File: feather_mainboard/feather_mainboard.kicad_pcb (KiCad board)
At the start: 2 copper layers, 0 parts

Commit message: added daughter board
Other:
- board outline added: 60 x 60 mm
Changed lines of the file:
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@@
 				(material "Peters SD2692")
 			)
-			(copper_finish "HAL lead-free")
+			(copper_finish "ENIG")
 			(dielectric_constraints no)
 		)
@@
 	)
 	(net 0 "")
+	(gr_line
+		(start 170 125)
+		(end 110 125)
+		(stroke
+			(width 0.05)
+			(type default)
+		)
+		(layer "Edge.Cuts")
+	)
+	(gr_line
+		(start 110 65)
+		(end 170 65)
+		(stroke
+			(width 0.05)
+			(type default)
+		)
+		(layer "Edge.Cuts")
+	)
+	(gr_line
+		(start 110 125)
+		(end 110 65)
+		(stroke
+			(width 0.05)
+			(type default)
+		)
+		(layer "Edge.Cuts")
+	)
+	(gr_line
+		(start 170 65)
+		(end 170 125)
+		(stroke
+			(width 0.05)
+			(type default)
+		)
+		(layer "Edge.Cuts")
+	)
 )

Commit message: finished mainboard design, need to do the routing
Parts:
- added C1_1: 100nF, Custom footprints:WCAP-CSGP_0603_R, F.Cu at (134.9, 107.7)
- added C1_2: 100nF, Custom footprints:WCAP-CSGP_0603_R, F.Cu at (131.7, 107.7)
- added C1_3: 100nF, Custom footprints:WCAP-CSGP_0603_R, F.Cu at (128.4, 107.8)
- added C1_4: 100nF, Custom footprints:WCAP-CSGP_0603_R, F.Cu at (139.7, 80.8)
- added C2_1: 10µF, Custom footprints:WCAP-CSGP_1210_H2.0, F.Cu at (167.1, 82.3)
- added C2_2: 10µF, Custom footprints:WCAP-CSGP_0603_R, F.Cu at (139.7, 83.9)
- added C3: 470pF, Custom footprints:WCAP-CSMH_1808_H2.0, F.Cu at (160.6, 95.6)
- added C4_1: 4.7µF, Custom footprints:WCAP-CSGP_1210_H2.0, F.Cu at (151.9, 95.3)
- added C4_2: 4.7µF, Custom footprints:WCAP-CSGP_1210_H2.0, F.Cu at (145.5, 81.7)
- added G***: LOGO, Custom footprints:Logo, F.Cu at (147.5, 72.9)
- added G***: LOGO, Custom footprints:Logo, B.Cu at (147.4, 72.9)
- added H1: MountingHole_Pad, MountingHole:MountingHole_2.2mm_M2_DIN965_Pad, F.Cu at (176.6, 73.1)
- added H2: MountingHole_Pad, MountingHole:MountingHole_2.2mm_M2_DIN965_Pad, F.Cu at (123.4, 73.1)
- added H3: MountingHole_Pad, MountingHole:MountingHole_2.2mm_M2_DIN965_Pad, F.Cu at (176.6, 126.3)
- added H4: MountingHole_Pad, MountingHole:MountingHole_2.2mm_M2_DIN965_Pad, F.Cu at (123.4, 126.3)
- added IIC: 61300211121, Custom footprints:61300211121, F.Cu at (172.5, 82.8)
- added J1: 61900819521, Custom footprints:61900819521, F.Cu at (160.9, 71.8)
- added J2: 61900619521, Custom footprints:61900619521, F.Cu at (136.4, 71.8)
- added J4: 693071020811, Custom footprints:693071020811, F.Cu at (124.3, 89.4)
- added L1: 6.8µH, Custom footprints:WE-PD2_4532, F.Cu at (146.2, 89.2)
- added R1_1: 10kΩ, Custom footprints:WRIS-RSKS_0603_REFLOW, F.Cu at (162.1, 107.5)
- added R1_10: 10kΩ, Custom footprints:WRIS-RSKS_0603_REFLOW, F.Cu at (140.4, 115.8)
- added R1_11: 10kΩ, Custom footprints:WRIS-RSKS_0603_REFLOW, F.Cu at (143.4, 115.8)
- added R1_2: 10kΩ, Custom footprints:WRIS-RSKS_0603_REFLOW, F.Cu at (144.9, 107.6)
- added R1_3: 10kΩ, Custom footprints:WRIS-RSKS_0603_REFLOW, F.Cu at (150.4, 115.8)
- added R1_4: 10kΩ, Custom footprints:WRIS-RSKS_0603_REFLOW, F.Cu at (153.4, 115.8)
- added R1_5: 10kΩ, Custom footprints:WRIS-RSKS_0603_REFLOW, F.Cu at (159.1, 115.8)
- added R1_6: 10kΩ, Custom footprints:WRIS-RSKS_0603_REFLOW, F.Cu at (128.4, 115.8)
- added R1_7: 10kΩ, Custom footprints:WRIS-RSKS_0603_REFLOW, F.Cu at (131.4, 115.8)
- added R1_8: 10kΩ, Custom footprints:WRIS-RSKS_0603_REFLOW, F.Cu at (134.4, 115.8)
- added R1_9: 10kΩ, Custom footprints:WRIS-RSKS_0603_REFLOW, F.Cu at (137.4, 115.8)
- added R2_1: 180Ω, Custom footprints:WRIS-RSKS_0603_REFLOW, F.Cu at (147.9, 107.6)
- added R3_1: 75kΩ, Custom footprints:WRIS-RSKS_0603_REFLOW, F.Cu at (162.1, 115.8)
- added RST: 61300211121, Custom footprints:61300211121, F.Cu at (144.3, 96.6)
- added S1: 450406020024, Custom footprints:450406020024, F.Cu at (169.8, 92.2)
- added SD: 61300211121, Custom footprints:61300211121, F.Cu at (139.8, 89.7)
- added U1: Adafruit ESP32-S3 Feather, Custom footprints:Adafruit ESP32-S3 Feather 4MB Flash 2MB PSRAM, F.Cu at (144.4, 95.7)
- added U2: SI2307CDS-T1-BE3, Custom footprints:SOT-23_VIS, F.Cu at (157.8, 107.6)
- added U3: 2N7002K-T1-GE3, Custom footprints:SOT_02K-T1-GE3_VIS, F.Cu at (152.3, 107.6)
- added U4: WPME-FISM_SMT-8, Custom footprints:WPME-FISM_SMT-8_L13.2W11.4H7.25, F.Cu at (156.6, 86.4)
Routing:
- added copper zone on B.Cu, net GND
- added copper zone on F.Cu, net GND
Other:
- board text added: "3.3V"
- board text added: "5V"
- board text added: "BUSY"
- board text added: "B_1"
- board text added: "B_2"
- board text added: "B_3"
- board text added: "B_4"
- board text added: "CLK"
- board text added: "CS"
- board text added: "DC"
- board text added: "DIN"
- board text added: "Do not connect"
- board text added: "GND"
- board text added: "IIC"
- board text added: "LPRD_Feather_MainBoard_V1"
- board text added: "RST"
- board text added: "SCL"
- board text added: "SDA"
- board text added: "TI_WiSe_2024/25"
- board text added: "VCC"

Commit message: finished the mainboard, added bom files
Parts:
- moved H2 0.36 mm to (123.2, 72.8)
- moved H4 0.36 mm to (123.2, 126.0)
- moved H1 0.36 mm to (176.4, 72.8)
- moved H3 0.36 mm to (176.4, 126.0)
- moved R1_1 0.30 mm to (162.4, 107.5)
- moved R1_5 0.30 mm to (159.4, 115.8)
- moved R1_6 0.30 mm to (128.7, 115.8)
- moved U1 0.30 mm to (144.7, 95.7)
- moved R1_2 0.30 mm to (145.2, 107.7)
- moved R2_1 0.30 mm to (148.2, 107.7)
- moved U2 0.30 mm to (158.1, 107.7)
- moved U3 0.30 mm to (152.6, 107.7)
- moved C1_1 0.30 mm to (135.2, 107.8)
- moved C1_2 0.30 mm to (131.9, 107.8)
- moved C1_3 0.30 mm to (128.7, 107.8)
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- renumbered G*** to G**
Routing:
- net /MicroSD-Card Adapter/SD_DAT1: track 0.00 -> 77.3 mm, vias 0 -> 1
- net /Display-Ports/SCLK: track 0.00 -> 71.9 mm, vias 0 -> 1
- net VCC: track 0.00 -> 68.4 mm
- net /MicroSD-Card Adapter/SD_CD: track 0.00 -> 68.4 mm, vias 0 -> 1
- net /Display-Ports/DIN: track 0.00 -> 67.9 mm
- net /Buttons-Connector/Button_1: track 0.00 -> 59.8 mm
- net /Buttons-Connector/Button_2: track 0.00 -> 57.3 mm
- net /Display-Enable/Switch: track 0.00 -> 56.8 mm
- net /Buttons-Connector/Button_4: track 0.00 -> 55.5 mm
- net /MicroSD-Card Adapter/SD_DAT2: track 0.00 -> 55.3 mm
- net /Display-Ports/RST: track 0.00 -> 55.2 mm
- net /Microcontroller/Reset: track 0.00 -> 54.8 mm
- net /Display-Ports/CS: track 0.00 -> 52.4 mm
- net /MicroSD-Card Adapter/SD_MOSI/DAT0: track 0.00 -> 52.0 mm, vias 0 -> 1
- net /Buttons-Connector/Button_3: track 0.00 -> 50.1 mm
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
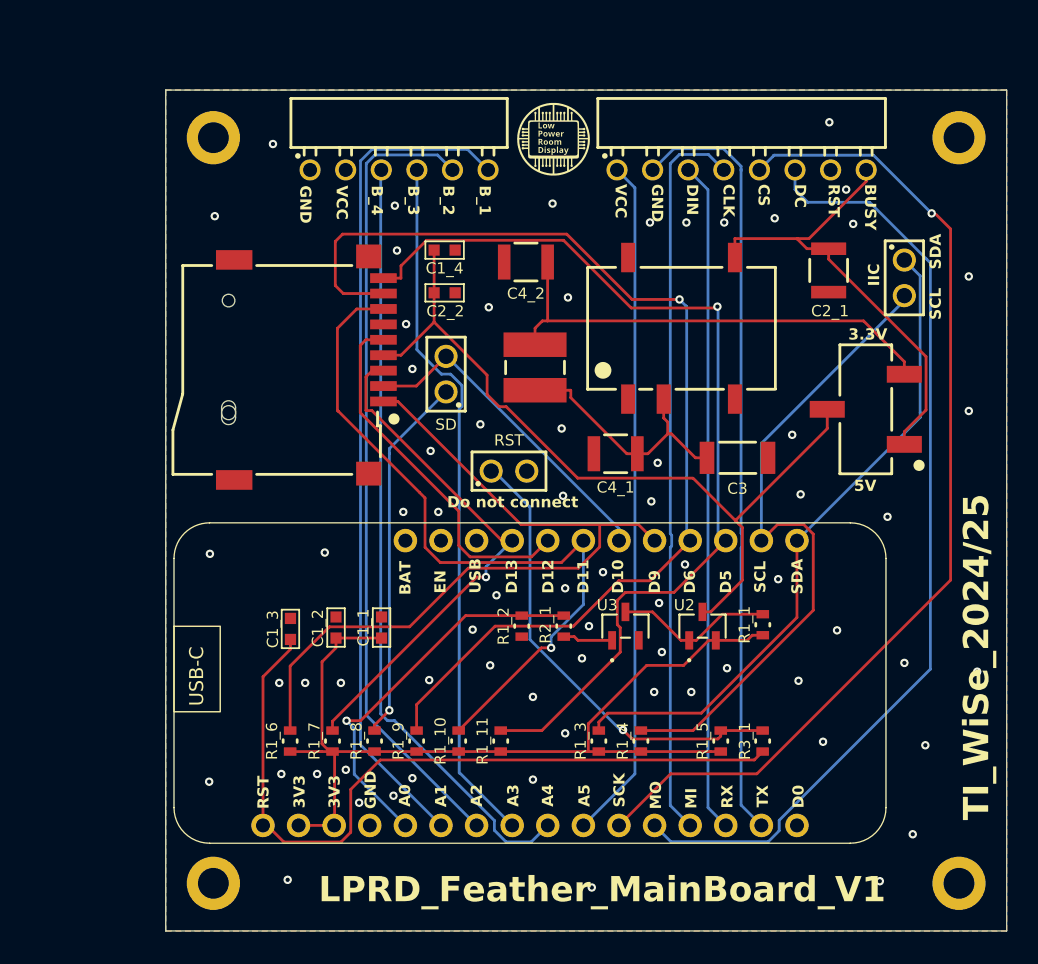
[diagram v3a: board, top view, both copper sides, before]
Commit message: moved the logo and did some small changes
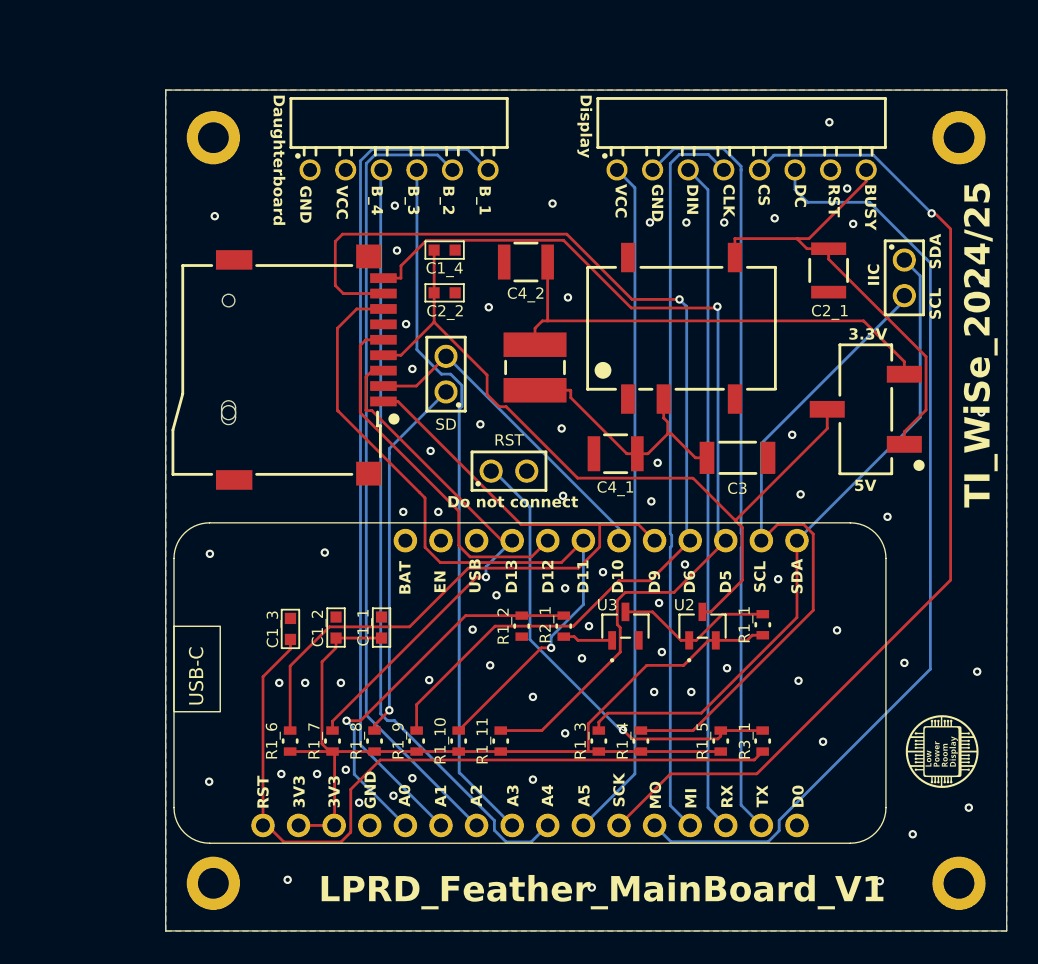
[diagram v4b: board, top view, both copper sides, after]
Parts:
- moved G*** 51.8 mm to (175.2, 116.6), turned to -90 degrees
- moved G** 51.7 mm to (175.2, 116.6), turned to 90 degrees
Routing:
- net GND: vias 69 -> 68
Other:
- board text added: "Daughterboard"
- board text added: "Display"

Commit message: added pins for the sd connections
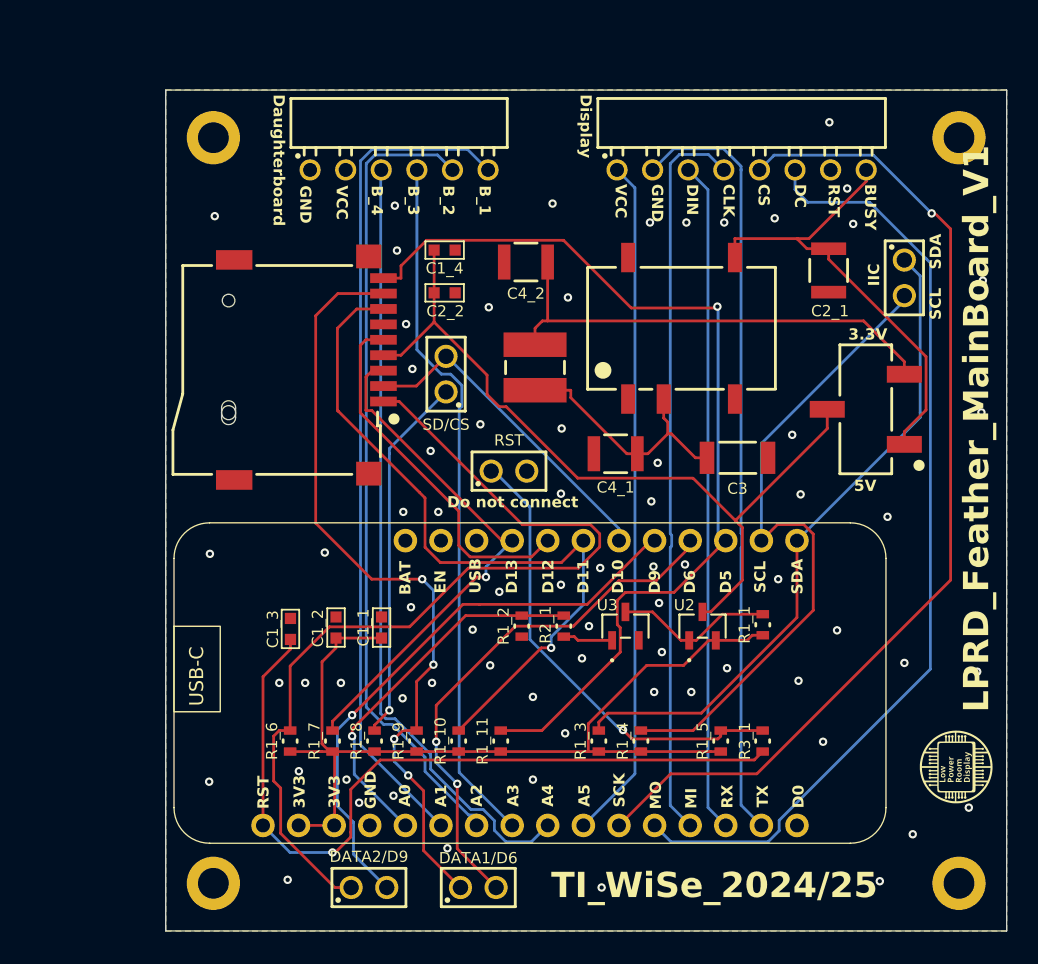
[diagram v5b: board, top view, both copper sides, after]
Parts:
- added DATA1/D6: 61300211121, Custom footprints:61300211121, F.Cu at (142.1, 126.3)
- added DATA2/D9: 61300211121, Custom footprints:61300211121, F.Cu at (134.3, 126.3)
- moved G** 1.49 mm to (176.2, 117.7)
- moved G*** 1.49 mm to (176.2, 117.7)
- renumbered SD to SD/CS
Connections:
- J4 pad 1: /MicroSD-Card Adapter/SD_DAT2 -> Net-(J4-DAT2)
- J4 pad 8: /MicroSD-Card Adapter/SD_DAT1 -> Net-(J4-DAT1)
- R1_6 pad 1: /MicroSD-Card Adapter/SD_DAT2 -> Net-(J4-DAT2)
- R1_9 pad 2: /MicroSD-Card Adapter/SD_DAT1 -> Net-(J4-DAT1)
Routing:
- net Net-(J4-DAT2): track 0.00 -> 65.6 mm
- net Net-(J4-DAT1): track 0.00 -> 55.6 mm, vias 0 -> 4
- net /MicroSD-Card Adapter/SD_DAT1: track 77.3 -> 38.4 mm, vias 1 -> 2
- net /MicroSD-Card Adapter/SD_DAT2: track 55.3 -> 40.9 mm, vias 0 -> 1
- net /Display-Enable/EN: track 28.0 -> 27.1 mm
- net /Buttons-Connector/Button_2: track 57.3 -> 58.0 mm
- net /Microcontroller/Reset: track 54.8 -> 55.5 mm, vias 0 -> 1
- net /Buttons-Connector/Button_4: track 55.5 -> 56.1 mm
- net GND: vias 68 -> 70

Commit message: changed the connector on the daughter board
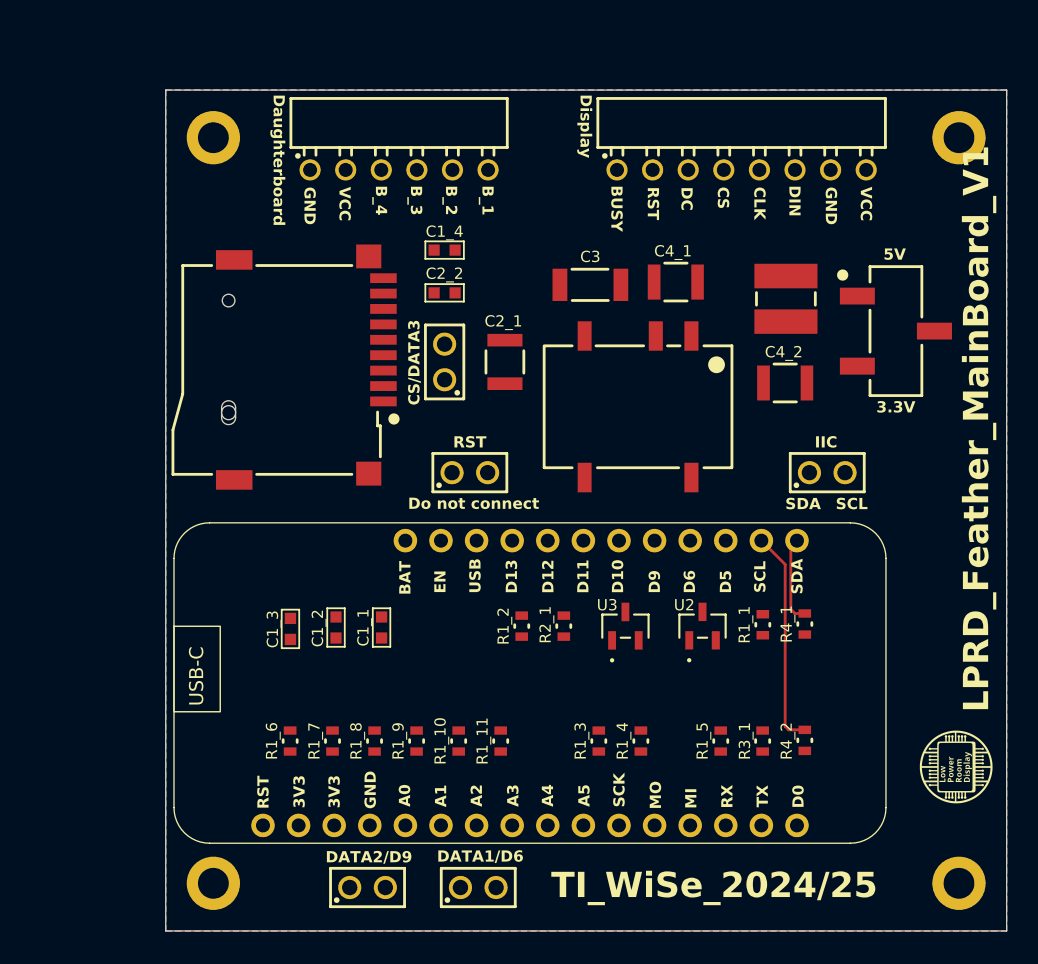
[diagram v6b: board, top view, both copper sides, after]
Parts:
- removed DATA1/D6, DATA2/D9, IIC, RST, SD/CS: 61300211121, Custom footprints:61300211121
- added J3: 61300211121, Custom footprints:61300211121, F.Cu at (141.5, 96.7)
- added J5: 61300211121, Custom footprints:61300211121, F.Cu at (139.7, 88.8)
- added J6: 61300211121, Custom footprints:61300211121, F.Cu at (167.0, 96.7)
- added J7: 61300211121, Custom footprints:61300211121, F.Cu at (134.2, 126.3)
- added J8: 61300211121, Custom footprints:61300211121, F.Cu at (142.1, 126.3)
- added R4_1: 33Ω, Custom footprints:WRIS-RSKS_0603_REFLOW, F.Cu at (165.4, 107.5)
- added R4_2: 33Ω, Custom footprints:WRIS-RSKS_0603_REFLOW, F.Cu at (165.4, 115.8)
- moved C2_1 24.0 mm to (144.0, 88.8), turned to 90 degrees
- moved C4_2 20.4 mm to (164.0, 90.3)
- moved L1 18.6 mm to (164.1, 84.3)
- moved C3 16.2 mm to (150.1, 83.3), turned to 180 degrees
- moved C4_1 13.0 mm to (156.2, 83.1), turned to 0 degrees
- moved U4 6.40 mm to (153.5, 92.0), turned to 180 degrees
- moved S1 5.98 mm to (171.9, 86.6), turned to -90 degrees
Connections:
- J2 pad 1: /Buttons-Connector/GND -> GND
- J2 pad 2: /Buttons-Connector/VCC -> VCC
- R1_3 pad 1: /IIC/SDA -> Net-(J6-Pad1)
- R1_4 pad 1: /IIC/SCL -> Net-(J6-Pad2)
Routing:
- net /Display-Ports/SCLK: track 71.9 -> 0.00 mm, vias 1 -> 0
- net VCC: track 68.4 -> 0.00 mm
- net /MicroSD-Card Adapter/SD_CD: track 68.4 -> 0.00 mm, vias 1 -> 0
- net /Display-Ports/DIN: track 67.9 -> 0.00 mm
- net Net-(J4-DAT2): track 65.6 -> 0.00 mm
- net /Buttons-Connector/Button_1: track 59.8 -> 0.00 mm
- net /Buttons-Connector/Button_2: track 58.0 -> 0.00 mm
- net /Display-Enable/Switch: track 56.8 -> 0.00 mm
- net /Buttons-Connector/Button_4: track 56.1 -> 0.00 mm
- net Net-(J4-DAT1): track 55.6 -> 0.00 mm, vias 4 -> 0
- net /Microcontroller/Reset: track 55.5 -> 0.00 mm, vias 1 -> 0
- net /Display-Ports/RST: track 55.2 -> 0.00 mm
- net /Display-Ports/CS: track 52.4 -> 0.00 mm
- net /MicroSD-Card Adapter/SD_MOSI/DAT0: track 52.0 -> 0.00 mm, vias 1 -> 0
- net /Buttons-Connector/Button_3: track 50.1 -> 0.00 mm
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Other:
- board text added: "CS/DATA3"
- board text added: "DATA1/D6"
- board text added: "DATA2/D9"

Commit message: finished mainboard and daughterboard
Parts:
- J1: value 61900819521 -> 62501021721; footprint Custom footprints:61900819521 -> Custom footprints:62501021721
- J2: value 61900619521 -> 62501021721; footprint Custom footprints:61900619521 -> Custom footprints:62501021721
- moved J1 1.27 mm to (162.1, 72.2)
- moved J2 1.12 mm to (137.5, 72.2)
- moved C4_1 0.10 mm to (156.3, 83.1)
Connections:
- J1 pad 1: /Display-Ports/BUSY -> unconnected-(J1-Pad1)
- J1 pad 2: /Display-Ports/RST -> /Display-Ports/BUSY
- J1 pad 3: /Display-Ports/DC -> /Display-Ports/RST
- J1 pad 4: /Display-Ports/CS -> /Display-Ports/DC
- J1 pad 5: /Display-Ports/SCLK -> /Display-Ports/CS
- J1 pad 6: /Display-Ports/DIN -> /Display-Ports/SCLK
- J1 pad 7: GND -> /Display-Ports/DIN
- J1 pad 8: /Boost-Converter/VOUT+ -> GND
- J2 pad 1: GND -> unconnected-(J2-Pad1)
- J2 pad 2: VCC -> unconnected-(J2-Pad2)
- J2 pad 4: /Buttons-Connector/Button_3 -> GND
- J2 pad 5: /Buttons-Connector/Button_2 -> /Buttons-Connector/Button_3
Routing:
- net VCC: track 0.00 -> 142.3 mm
- net /Display-Enable/Switch: track 0.00 -> 91.9 mm
- net /Buttons-Connector/Button_4: track 0.00 -> 64.0 mm
- net /Microcontroller/Reset: track 0.00 -> 58.9 mm
- net /Display-Ports/DIN: track 0.00 -> 57.9 mm
- net /Display-Ports/SCLK: track 0.00 -> 54.3 mm
- net /MicroSD-Card Adapter/SD_CD: track 0.00 -> 54.2 mm
- net /Display-Ports/CS: track 0.00 -> 52.3 mm
- net Net-(J4-DAT1): track 0.00 -> 51.5 mm, vias 0 -> 3
- net /Display-Ports/BUSY: track 0.00 -> 50.8 mm
- net /Buttons-Connector/Button_1: track 0.00 -> 48.4 mm
- net /Display-Ports/DC: track 0.00 -> 47.3 mm
- net /Buttons-Connector/Button_3: track 0.00 -> 47.1 mm, vias 0 -> 1
- net /Buttons-Connector/Button_2: track 0.00 -> 46.7 mm
- net /Display-Ports/RST: track 0.00 -> 45.1 mm
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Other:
- board text added: "bklaric"
- board text removed: "BUSY"
- board text removed: "B_1"
- board text removed: "B_2"
- board text removed: "B_3"
- board text removed: "B_4"
- board text removed: "CLK"
- board text removed: "CS"
- board text removed: "DC"
- board text removed: "DIN"
- board text removed: "GND"
- board text removed: "VCC"
